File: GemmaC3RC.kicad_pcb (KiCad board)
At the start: 2 copper layers, 30.7 x 56 mm, 14 parts, among them J1 I2C_CH0, J2 I2C_CH1, J3 DC-Motor, J4 3.7V Battery, J5 Servo, J6 Pot, J7 Pot, J8 Ext1, J9 Ext2, U1 ESP32-C3_SUPERMINI

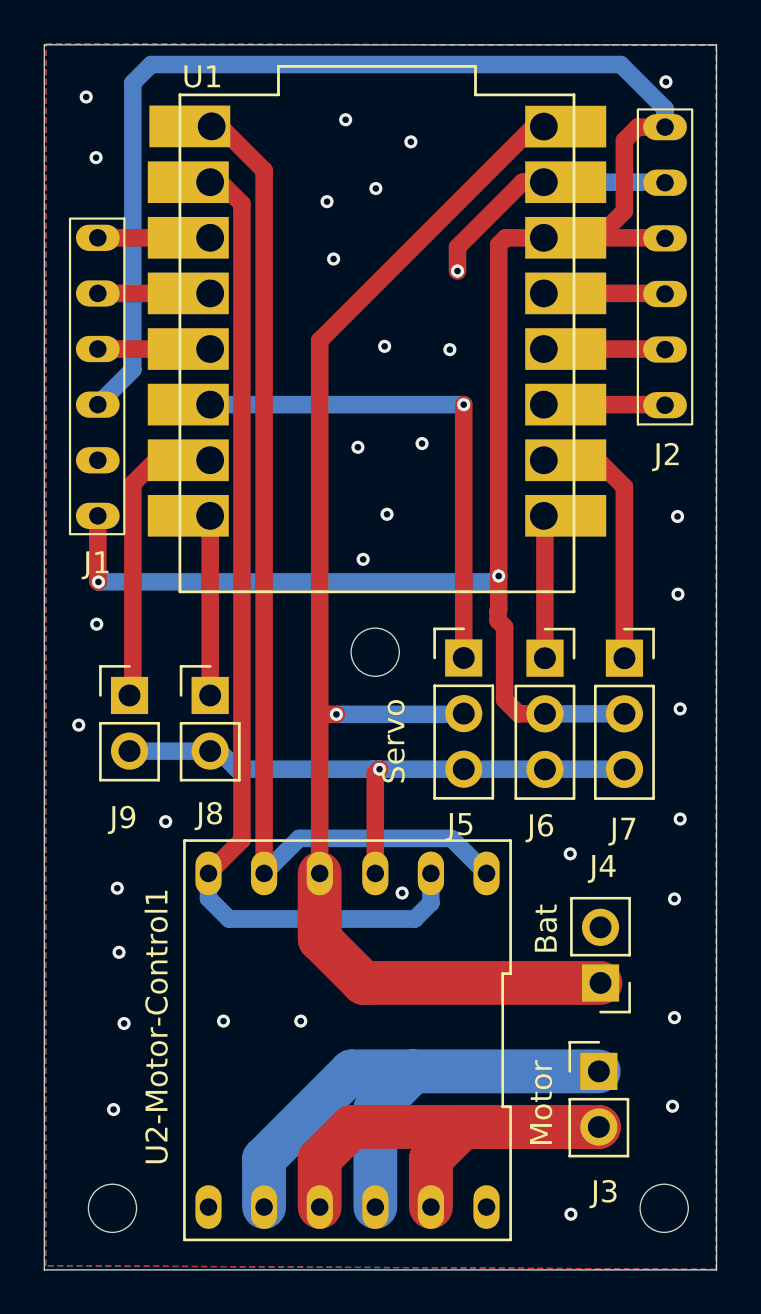
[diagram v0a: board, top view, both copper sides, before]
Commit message: Updated to ver 1.1
Bat is conneced to 3.3V and In1 io pin changed
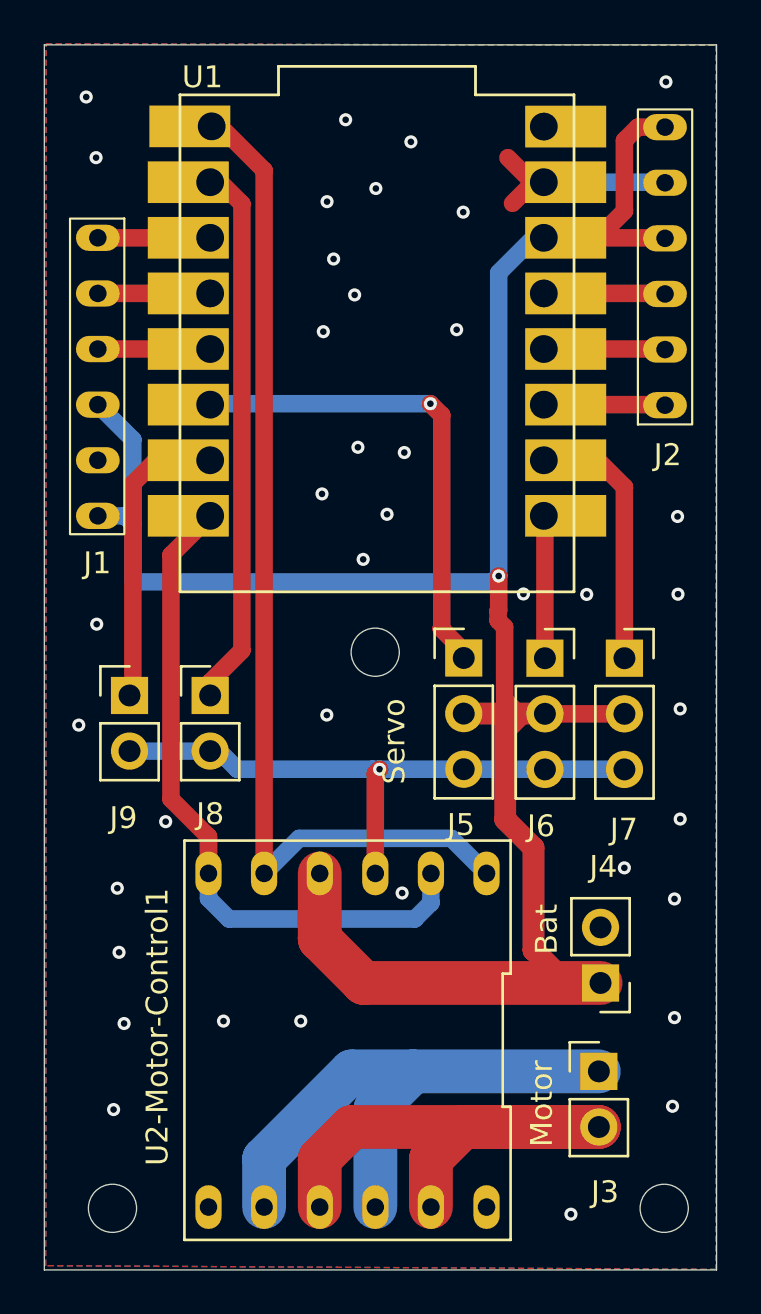
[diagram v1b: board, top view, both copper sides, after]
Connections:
- J4 pad 1: +BATT -> +3.3V
- J5 pad 2: +BATT -> +3.3V
- J8 pad 1: /GP21 -> Net-(J8-Pin_1)
- U1 pad 5V: +BATT -> unconnected-(U1-Pad5V)
- U1 pad 6: /MC_1 -> Net-(J8-Pin_1)
- U2-Motor-Control1 pad 2: /MC_1 -> /GP21
- U2-Motor-Control1 pad 4: +BATT -> +3.3V
- U2-Motor-Control1 pad 6: /MC_1 -> /GP21
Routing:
- net +BATT: track 62.0 -> 0.00 mm, vias 1 -> 0
- net /MC_1: track 46.4 -> 0.00 mm
- net Net-(J8-Pin_1): track 0.00 -> 24.9 mm
- net /GP21: track 8.20 -> 31.1 mm
- net GND: track 39.8 -> 37.5 mm, vias 35 -> 40
- net /Servo_SIGN: track 23.4 -> 22.6 mm
- net +3.3V: track 106.3 -> 107.1 mm, vias 2 -> 1
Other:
- board text added: "USN GEMMA-RC C3 Ver 1.1"
- board text removed: "USN GEMMA-RC C3 Ver 1.0"
